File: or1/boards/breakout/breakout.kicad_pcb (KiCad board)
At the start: 4 copper layers, 50 x 36 mm, 16 parts, among them J1 CONN_SKY130_TEST_DEVICE, U1 SKY130_TEST_OR1

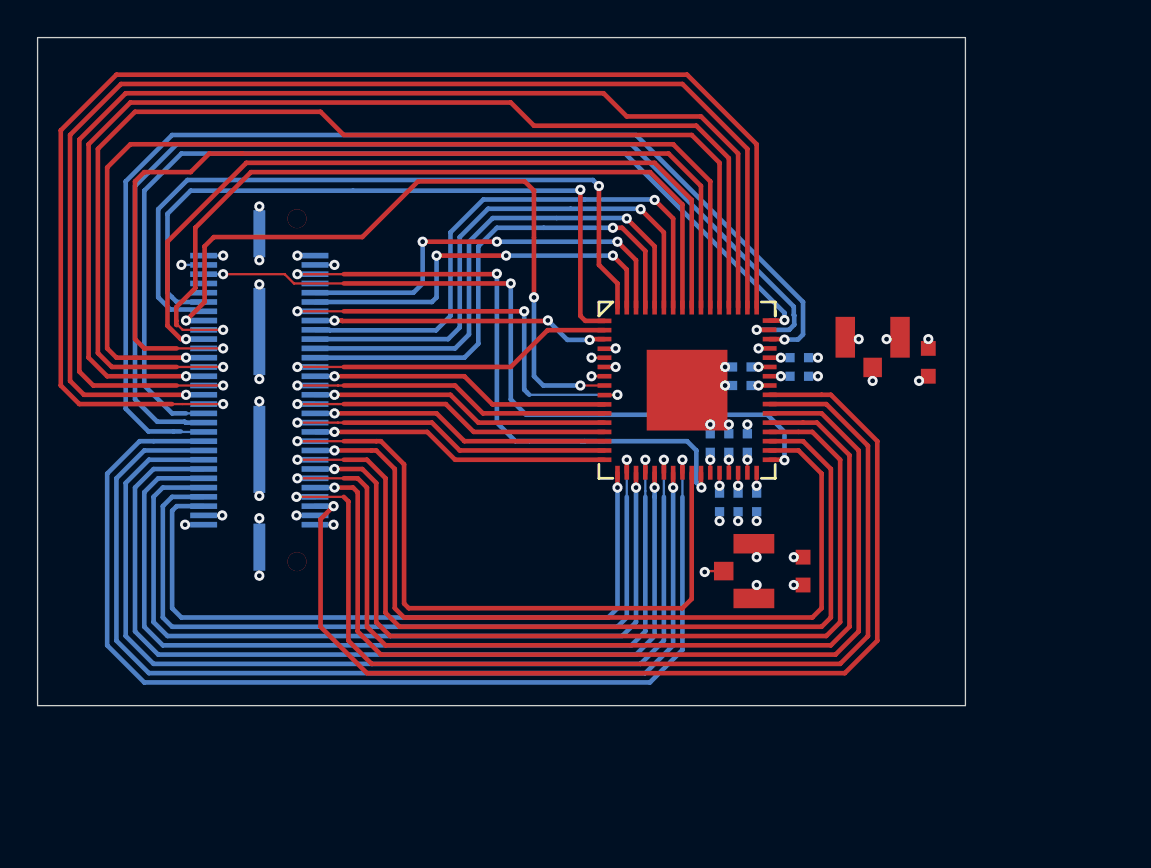
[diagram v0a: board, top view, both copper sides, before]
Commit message: Finished initial routing. Ready for layout review.
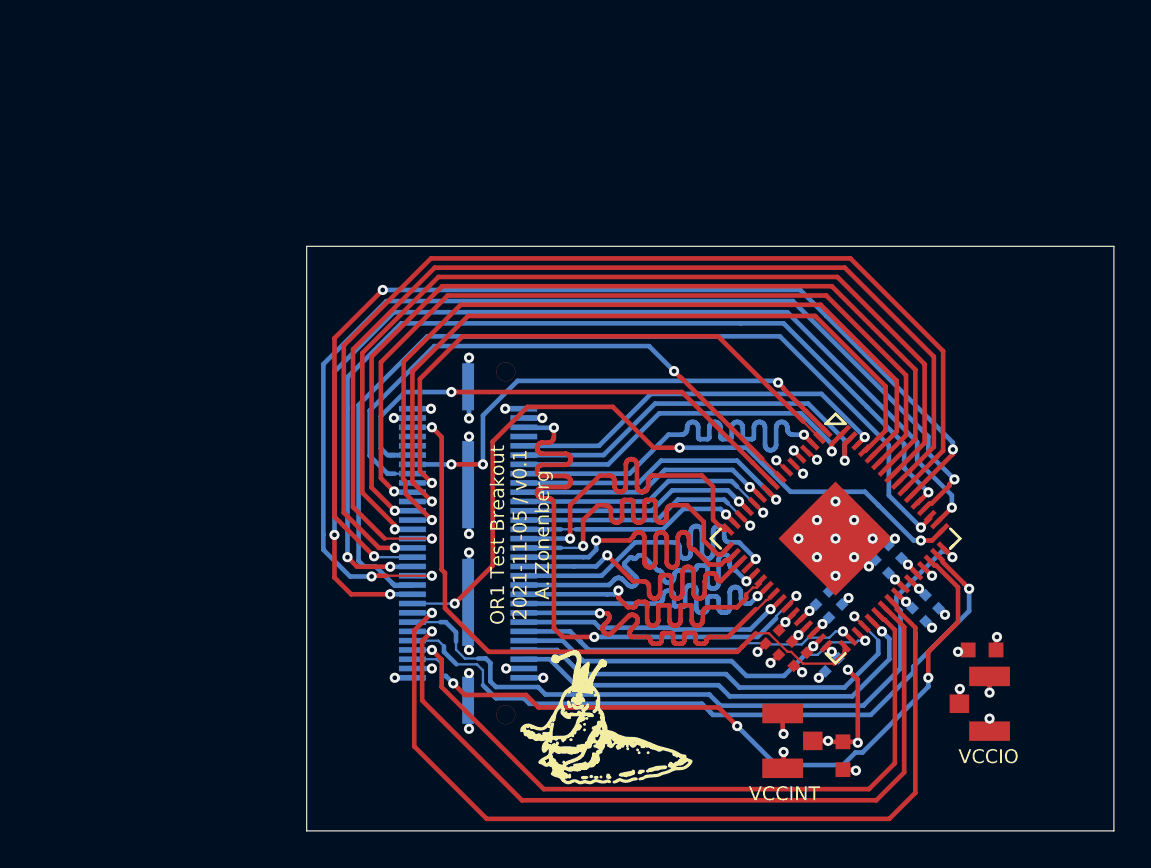
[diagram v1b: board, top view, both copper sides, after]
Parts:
- added G***: LOGO, azonenberg_pcb:LONGTHING-1200DPI, F.Cu at (52.2, 71.0)
- C5, C6, C8: moved to F.Cu
- moved TP1 20.6 mm to (72.2, 70.0), turned to 270 degrees
- moved C7 16.4 mm to (68.5, 65.2), turned to 315 degrees
- moved C1 15.8 mm to (72.0, 67.0), turned to 180 degrees
- moved C9 15.0 mm to (69.2, 64.5), turned to 315 degrees
- moved J1 14.0 mm to (44.2, 61.3)
- moved C4 13.2 mm to (63.9, 67.8), turned to 225 degrees
- moved C11 12.2 mm to (67.2, 61.8), turned to 135 degrees
- moved C6 12.0 mm to (62.1, 67.5), turned to 225 degrees
- moved U1 11.3 mm to (64.0, 61.0), turned to 315 degrees
- moved C3 11.2 mm to (66.5, 62.5), turned to 135 degrees
- moved C5 11.0 mm to (60.6, 66.3), turned to 225 degrees
- moved C2 10.2 mm to (64.5, 72.8), turned to 270 degrees
- moved TP2 9.32 mm to (61.3, 72.0), turned to 90 degrees
- moved C8 8.62 mm to (61.4, 67.0), turned to 225 degrees
- moved C12 7.23 mm to (64.0, 65.0), turned to 45 degrees
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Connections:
- J1 pad 10: /DOUT1[31] -> /DIN0[31]
- J1 pad 11: /ADDR1[4] -> /ADDR1[1]
- J1 pad 12: /DOUT1[24] -> /ADDR1[6]
- J1 pad 13: /ADDR1[3] -> /ADDR1[0]
- J1 pad 14: /DOUT1[23] -> /DOUT0[24]
- J1 pad 15: /ADDR1[2] -> /DOUT1[0]
- J1 pad 16: /DOUT1[16] -> /ADDR1[7]
- J1 pad 17: /ADDR1[1] -> /DOUT1[15]
- J1 pad 18: /DOUT1[15] -> /DIN0[24]
- J1 pad 19: /ADDR1[0] -> /DOUT1[16]
- J1 pad 20: /DOUT1[0] -> /DOUT0[23]
- J1 pad 21: /ADDR0[7] -> /DOUT1[23]
- J1 pad 22: /DOUT0[31] -> /DIN0[23]
- J1 pad 23: /ADDR0[6] -> /DOUT1[24]
- J1 pad 24: /DIN0[31] -> /DOUT0[16]
- J1 pad 25: /ADDR0[5] -> /DOUT1[31]
- J1 pad 26: /DOUT0[24] -> /DIN0[16]
- J1 pad 27: /ADDR0[4] -> /DOUT1[7]
- J1 pad 28: /DIN0[24] -> /DOUT0[15]
- J1 pad 29: /ADDR0[3] -> /DOUT1[8]
- J1 pad 30: /DOUT0[23] -> /DIN0[15]
- J1 pad 31: /ADDR0[2] -> /ADDR0[7]
- J1 pad 32: /DIN0[23] -> /DIN0[8]
- J1 pad 33: /ADDR0[1] -> /ADDR0[6]
- J1 pad 34: /DOUT0[16] -> /DOUT0[8]
- J1 pad 35: /ADDR0[0] -> /ADDR0[5]
- J1 pad 36: /DIN0[16] -> /DOUT0[0]
- J1 pad 37: /DIN0[0] -> /ADDR0[4]
- J1 pad 38: /DOUT0[15] -> /DIN0[7]
- J1 pad 39: /DOUT0[0] -> /ADDR0[3]
- J1 pad 40: /DIN0[15] -> /DIN0[0]
- J1 pad 41: /DOUT0[7] -> /ADDR0[2]
- J1 pad 42: /DIN0[8] -> /DOUT0[7]
- J1 pad 43: /DIN0[7] -> /ADDR0[1]
- J1 pad 44: /DOUT0[8] -> /ADDR0[0]
- J1 pad 47: /WE0_N -> /WMASK0[2]
- J1 pad 48: /WMASK0[2] -> /WMASK0[3]
- J1 pad 5: /ADDR1[7] -> /ADDR1[4]
- J1 pad 50: /WMASK0[3] -> /WE0_N
- J1 pad 6: /DOUT1[8] -> /DOUT0[31]
- J1 pad 7: /ADDR1[6] -> /ADDR1[3]
- J1 pad 8: /DOUT1[7] -> /ADDR1[5]
- J1 pad 9: /ADDR1[5] -> /ADDR1[2]
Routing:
- net /DOUT1[0]: track 58.7 -> 20.1 mm
- net /DOUT1[15]: track 54.7 -> 20.0 mm
- net /DOUT1[16]: track 53.6 -> 20.0 mm
- net /DIN0[24]: track 73.1 -> 40.1 mm, vias 1 -> 3
- net /ADDR1[4]: track 53.5 -> 23.9 mm
- net /DOUT1[23]: track 49.6 -> 20.0 mm
- net /ADDR1[2]: track 49.8 -> 20.6 mm
- net /DOUT1[24]: track 48.4 -> 20.0 mm
- net /ADDR1[1]: track 46.2 -> 18.7 mm
- net /ADDR1[3]: track 49.9 -> 24.0 mm
- net /DOUT1[31]: track 44.3 -> 20.1 mm
- net /DOUT1[7]: track 43.0 -> 20.0 mm
- net /ADDR1[0]: track 37.3 -> 14.6 mm
- net /DOUT0[31]: track 61.9 -> 40.4 mm, vias 1 -> 3
- net /DIN0[31]: track 59.6 -> 38.6 mm
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- added copper zone on In1.Cu, net /GND
- added copper zone on In2.Cu, net /VCCINT
- added copper zone on In2.Cu, net /VCCIO
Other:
- board size 50 x 36 mm -> 43.5 x 31.5 mm
- board text added: "OR1 Test Breakout 2021-11-05 / v0.1 A. Zonenberg"
- board text added: "VCCINT"
- board text added: "VCCIO"

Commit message: Final rev of breakout ready for fab
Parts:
- removed G***: LOGO, azonenberg_pcb:LONGTHING-1200DPI
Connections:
- J1 pad 20: /DOUT0[23] -> /DOUT0[16]
- J1 pad 24: /DOUT0[16] -> /DOUT0[23]
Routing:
- net /CLK1: track 35.0 -> 26.5 mm
- net /VCCINT: track 50.4 -> 57.9 mm
- net /DIN0[23]: track 51.5 -> 45.0 mm
- net /DOUT0[16]: track 59.9 -> 55.4 mm, vias 3 -> 1
- net /DOUT0[23]: track 56.8 -> 52.5 mm, vias 3 -> 1
- net /WE0_N: track 28.5 -> 24.5 mm
- net /CS0_N: track 31.6 -> 28.2 mm
- net /DIN0[16]: track 51.3 -> 48.2 mm, vias 3 -> 1
- net /DOUT0[0]: track 44.5 -> 41.5 mm
- net /DOUT0[7]: track 45.2 -> 42.3 mm
- net /DIN0[0]: track 40.8 -> 38.0 mm
- net /DIN0[7]: track 48.6 -> 46.1 mm
- net /DOUT0[8]: track 52.0 -> 49.9 mm
- net /DOUT0[15]: track 56.4 -> 54.4 mm
- net /DIN0[8]: track 57.3 -> 55.3 mm
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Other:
- board text added: "OR1 Test Breakout 2021-11-06 / v0.1 A. Zonenberg"
- board text added: "Serial number label here"
- board text removed: "OR1 Test Breakout 2021-11-05 / v0.1 A. Zonenberg"
